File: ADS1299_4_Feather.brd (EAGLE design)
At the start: 90 x 40 mm, 40 parts, among them U1 ADS1299-4PAG

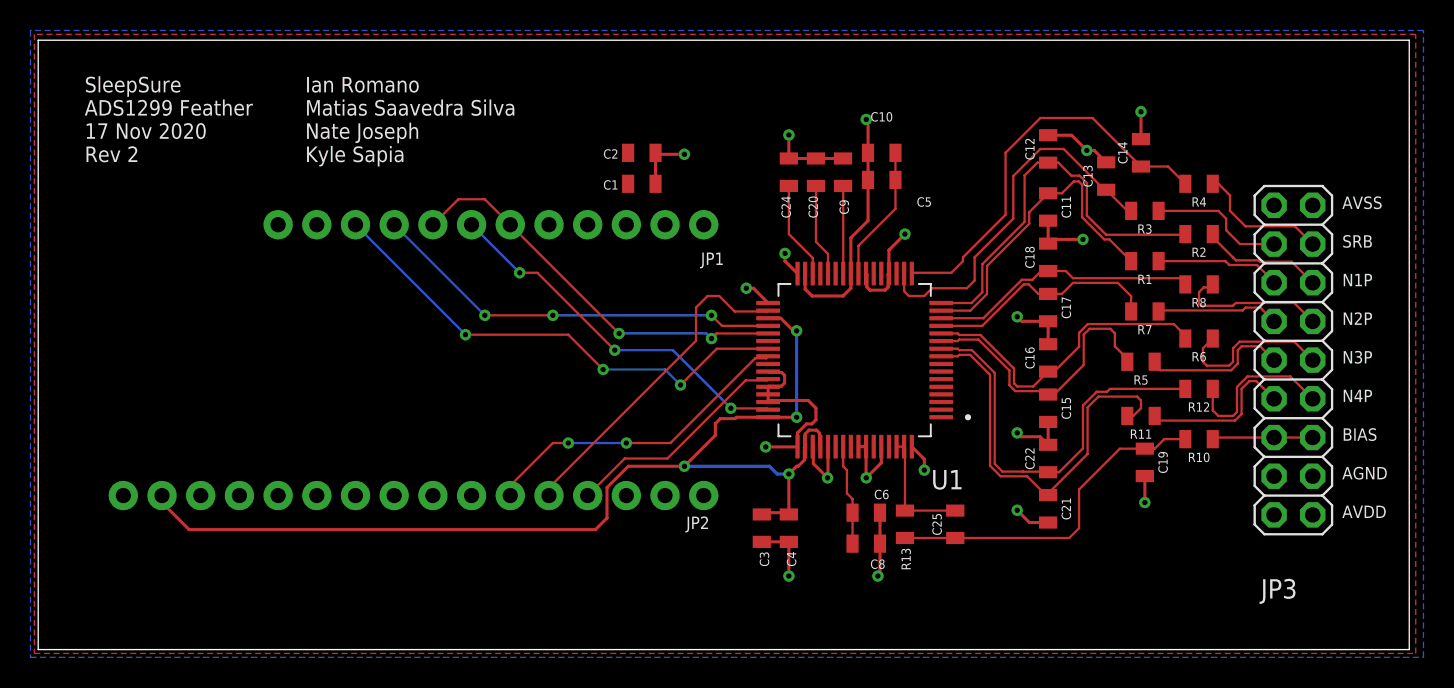
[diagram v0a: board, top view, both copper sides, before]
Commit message: Increased distance between adafruit mounting headers from 0.7" to 0.8"
	modified:   ADS1299_4_Feather.brd
	modified:   ADS1299_4_Feather.sch
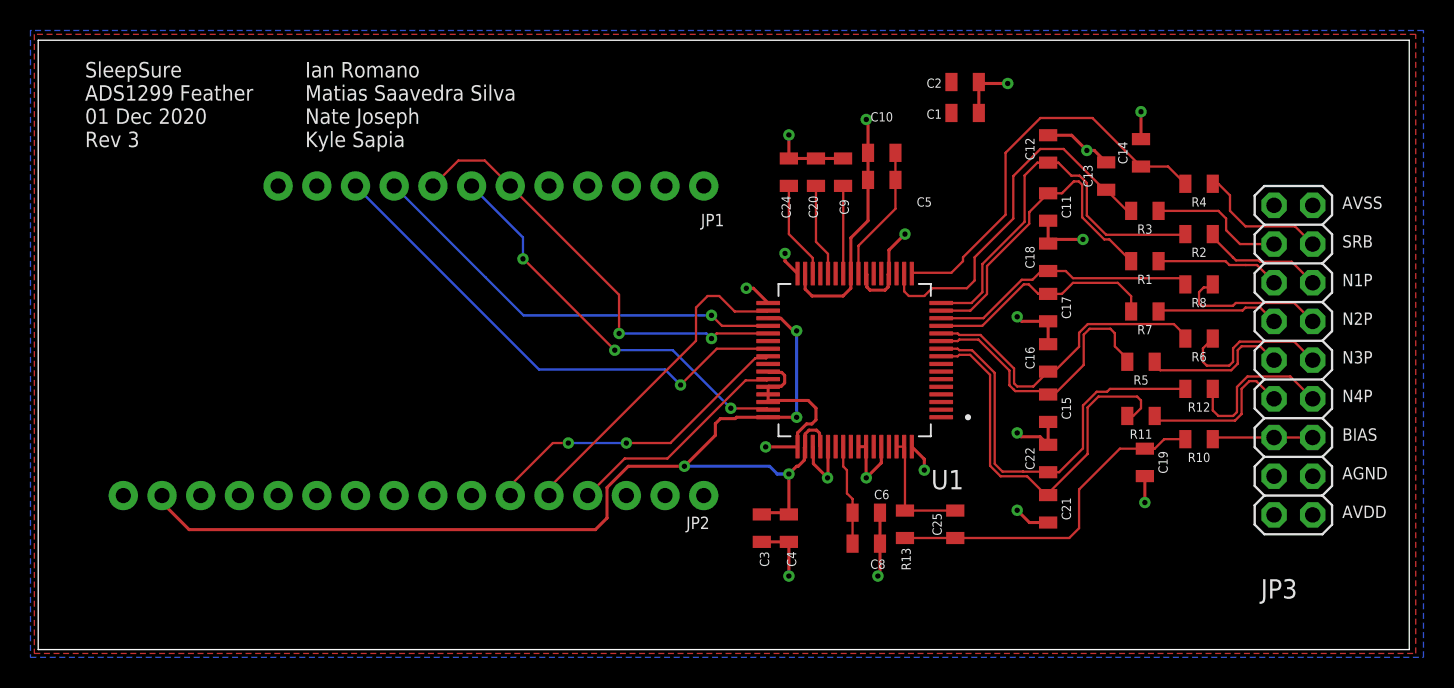
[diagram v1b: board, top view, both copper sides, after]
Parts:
- moved C1 21.7 mm to (60.8, 35.2)
- moved C2 21.7 mm to (60.8, 37.3)
- moved JP1 2.54 mm to (29.7, 30.4)
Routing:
- net CLK0: track 26.6 -> 29.2 mm
- net DRDY: track 24.5 -> 26.4 mm
- net ADS_RESET: track 27.3 -> 28.3 mm, vias 3 -> 1
- net CS1: track 32.4 -> 33.5 mm, vias 3 -> 1
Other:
- board text added: "SleepSure ADS1299 Feather 01 Dec 2020 Rev 3"
- board text removed: "SleepSure ADS1299 Feather 17 Nov 2020 Rev 2"
